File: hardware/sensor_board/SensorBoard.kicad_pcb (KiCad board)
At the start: 2 copper layers, 89.5 x 80 mm, 26 parts, among them J1 EXT, J10 LED L1, J11 LED R3, J12 LED R2, J13 LED R1, J14 HX711 L, J15 HX711 R, J2 TARE L, J3 TARE R, J4 SOIL SENSOR L, J5 SOIL SENSOR R, J6 DHT22 L, J7 DHT22 R, J8 LED L3, J9 LED L2, U1 Pico

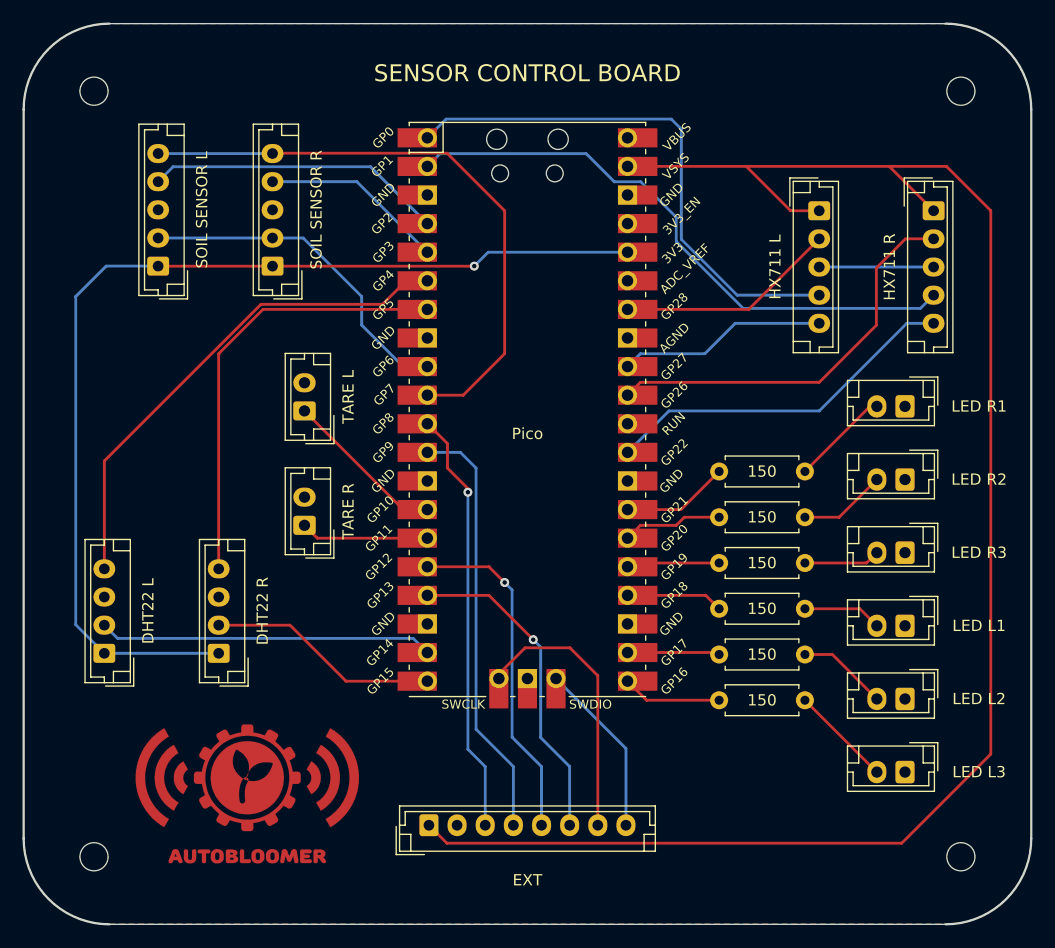
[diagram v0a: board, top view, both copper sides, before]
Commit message: PCB v2.0. Using sonars instead of load cells, which frees up the tare buttons. Also using a shift register for LEDs instead of direct GPIO control which frees up three more pins.
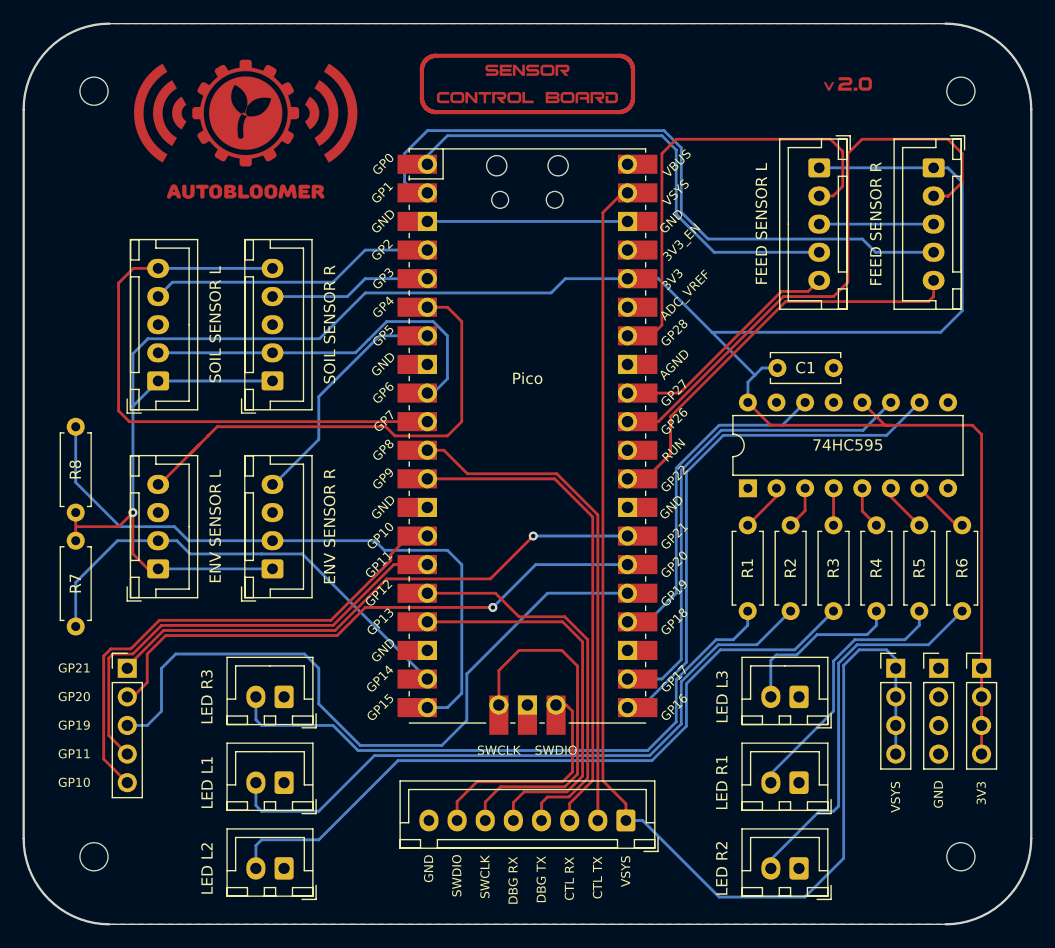
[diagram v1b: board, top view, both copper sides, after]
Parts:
- removed the J2 at (114.3, 83.8)
- removed the J3 at (114.3, 94.0)
- added C1: 0.1uf, Capacitor_THT:C_Disc_D6.0mm_W2.5mm_P5.00mm, F.Cu at (156.3, 80.0)
- added J14: SPARE GPIO, Connector_PinHeader_2.54mm:PinHeader_1x05_P2.54mm_Vertical, F.Cu at (98.6, 106.7)
- added J15: VSYS BUS, Connector_PinHeader_2.54mm:PinHeader_1x04_P2.54mm_Vertical, F.Cu at (166.8, 106.7)
- added J16: GND BUS, Connector_PinHeader_2.54mm:PinHeader_1x04_P2.54mm_Vertical, F.Cu at (170.6, 106.7)
- added J17: 3V3 BUS, Connector_PinHeader_2.54mm:PinHeader_1x04_P2.54mm_Vertical, F.Cu at (174.4, 106.7)
- added R7: R7, Resistor_THT:R_Axial_DIN0207_L6.3mm_D2.5mm_P7.62mm_Horizontal, F.Cu at (94.0, 103.0)
- added R8: R8, Resistor_THT:R_Axial_DIN0207_L6.3mm_D2.5mm_P7.62mm_Horizontal, F.Cu at (94.0, 85.2)
- added U2: 74HC595, Package_DIP:DIP-16_W7.62mm, F.Cu at (153.7, 90.7)
- J1: footprint Connector_JST:JST_EH_B8B-EH-A_1x08_P2.50mm_Vertical -> Connector_JST:JST_XH_B8B-XH-A_1x08_P2.50mm_Vertical
- J10: renamed from J11; value LED R3 -> LED L2; footprint Connector_JST:JST_EH_B2B-EH-A_1x02_P2.50mm_Vertical -> Connector_JST:JST_XH_B2B-XH-A_1x02_P2.50mm_Vertical
- J11: renamed from J10; value LED L1 -> LED L3; footprint Connector_JST:JST_EH_B2B-EH-A_1x02_P2.50mm_Vertical -> Connector_JST:JST_XH_B2B-XH-A_1x02_P2.50mm_Vertical
- J12: renamed from J9; value LED L2 -> LED R1; footprint Connector_JST:JST_EH_B2B-EH-A_1x02_P2.50mm_Vertical -> Connector_JST:JST_XH_B2B-XH-A_1x02_P2.50mm_Vertical
- J13: renamed from J8; value LED L3 -> LED R2; footprint Connector_JST:JST_EH_B2B-EH-A_1x02_P2.50mm_Vertical -> Connector_JST:JST_XH_B2B-XH-A_1x02_P2.50mm_Vertical
- J2: renamed from J4; footprint Connector_JST:JST_EH_B5B-EH-A_1x05_P2.50mm_Vertical -> Connector_JST:JST_XH_B5B-XH-A_1x05_P2.50mm_Vertical
- J3: renamed from J5; footprint Connector_JST:JST_EH_B5B-EH-A_1x05_P2.50mm_Vertical -> Connector_JST:JST_XH_B5B-XH-A_1x05_P2.50mm_Vertical
- J4: renamed from J6; value DHT22 L -> ENV SENSOR L; footprint Connector_JST:JST_EH_B4B-EH-A_1x04_P2.50mm_Vertical -> Connector_JST:JST_XH_B4B-XH-A_1x04_P2.50mm_Vertical
- J5: renamed from J7; value DHT22 R -> ENV SENSOR R; footprint Connector_JST:JST_EH_B4B-EH-A_1x04_P2.50mm_Vertical -> Connector_JST:JST_XH_B4B-XH-A_1x04_P2.50mm_Vertical
- J6: renamed from J14; value HX711 L -> FEED SENSOR L; footprint Connector_JST:JST_EH_B5B-EH-A_1x05_P2.50mm_Vertical -> Connector_JST:JST_XH_B5B-XH-A_1x05_P2.50mm_Vertical
- J7: renamed from J15; value HX711 R -> FEED SENSOR R; footprint Connector_JST:JST_EH_B5B-EH-A_1x05_P2.50mm_Vertical -> Connector_JST:JST_XH_B5B-XH-A_1x05_P2.50mm_Vertical
- J8: renamed from J13; value LED R1 -> LED R3; footprint Connector_JST:JST_EH_B2B-EH-A_1x02_P2.50mm_Vertical -> Connector_JST:JST_XH_B2B-XH-A_1x02_P2.50mm_Vertical
- J9: renamed from J12; value LED R2 -> LED L1; footprint Connector_JST:JST_EH_B2B-EH-A_1x02_P2.50mm_Vertical -> Connector_JST:JST_XH_B2B-XH-A_1x02_P2.50mm_Vertical
- R1: value 150 -> R1
- R2: value 150 -> R2
- R3: value 150 -> R3
- R4: value 150 -> R4
- R5: value 150 -> R5
- R6: value 150 -> R6
- moved J10 61.9 mm to (112.5, 124.5)
- moved J9 61.4 mm to (112.5, 116.8)
- moved J8 60.9 mm to (112.5, 109.2)
- moved R6 26.6 mm to (172.7, 94.0), turned to -90 degrees
- moved R5 21.2 mm to (168.9, 94.0), turned to -90 degrees
- moved J1 17.5 mm to (142.9, 120.2), turned to 180 degrees
- moved R4 15.8 mm to (165.1, 94.0), turned to -90 degrees
- moved J13 12.7 mm to (158.2, 124.5)
- moved J12 12.0 mm to (158.2, 116.8)
- moved J11 11.3 mm to (158.2, 109.2)
- moved R3 10.7 mm to (161.3, 94.0), turned to -90 degrees
- moved J2 10.2 mm to (101.3, 81.2)
- moved J3 10.2 mm to (111.5, 81.2)
- moved J4 8.89 mm to (101.3, 97.8)
- moved J5 8.89 mm to (111.5, 97.8)
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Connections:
- net Net-(J14-Pad2) renamed /FEED SENSOR L TX
- net Net-(J14-Pad4) renamed /FEED SENSOR L DETECT
- net Net-(J14-Pad5) renamed /FEED SENSOR L RX
- net Net-(J15-Pad2) renamed /FEED SENSOR R TX
- net Net-(J15-Pad4) renamed /FEED SENSOR R DETECT
- net Net-(J15-Pad5) renamed /FEED SENSOR R RX
- net Net-(J4-Pad2) renamed /I2C1 SDA
- net Net-(J4-Pad4) renamed /SOIL SENSOR L DETECT
- net Net-(J4-Pad5) renamed /I2C1 SCL
- net Net-(J5-Pad4) renamed /SOIL SENSOR R DETECT
- net Net-(J6-Pad2) renamed /ENV SENSOR L CTL
- net Net-(J6-Pad4) renamed /ENV SENSOR L DETECT
- net Net-(J7-Pad2) renamed /ENV SENSOR R CTL
- net Net-(J7-Pad4) renamed /ENV SENSOR R DETECT
- J1 pad 2: GND -> /CTL TX
- J1 pad 3: Net-(J1-Pad3) -> /CTL RX
- J1 pad 4: Net-(J1-Pad4) -> /DBG TX
- J1 pad 5: Net-(J1-Pad5) -> /DBG RX
- J1 pad 6: Net-(J1-Pad6) -> /SWCLK
- J1 pad 7: Net-(J1-Pad7) -> /SWDIO
- J1 pad 8: Net-(J1-Pad8) -> GND
- J2 pad 1: +3.3V -> +3V3
- J3 pad 1: +3.3V -> +3V3
- J4 pad 1: +3.3V -> +3V3
- J5 pad 1: +3.3V -> +3V3
- J6 pad 1: VS -> +3V3
- J7 pad 1: VS -> +3V3
- U1 pad 11: Net-(J1-Pad3) -> /CTL TX
- U1 pad 12: Net-(J1-Pad4) -> /CTL RX
- U1 pad 14: Net-(J2-Pad1) -> /GPIO10
- U1 pad 15: Net-(J3-Pad1) -> /GPIO11
- U1 pad 16: Net-(J1-Pad5) -> /DBG TX
- U1 pad 17: Net-(J1-Pad6) -> /DBG RX
- U1 pad 21: Net-(R6-Pad1) -> Net-(U1-Pad21)
- U1 pad 22: Net-(R5-Pad1) -> Net-(U1-Pad22)
- U1 pad 24: Net-(R4-Pad1) -> Net-(U1-Pad24)
- U1 pad 25: Net-(R3-Pad1) -> /GPIO19
- U1 pad 26: Net-(R2-Pad1) -> /GPIO20
- U1 pad 27: Net-(R1-Pad1) -> /GPIO21
- U1 pad 36: +3.3V -> +3V3
- U1 pad 41: Net-(J1-Pad7) -> /SWCLK
- U1 pad 43: Net-(J1-Pad8) -> /SWDIO
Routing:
- net +3V3: track 0.00 -> 221.2 mm, vias 0 -> 1
- net +3.3V: track 93.5 -> 0.00 mm, vias 1 -> 0
- net /GPIO19: track 0.00 -> 62.5 mm
- net Net-(J10-Pad2): track 6.77 -> 64.2 mm
- net Net-(J9-Pad2): track 7.78 -> 59.3 mm
- net /GPIO20: track 0.00 -> 50.3 mm, vias 0 -> 1
- net /GPIO21: track 0.00 -> 49.2 mm, vias 0 -> 1
- net Net-(U1-Pad21): track 0.00 -> 47.0 mm
- net Net-(J8-Pad2): track 8.78 -> 54.9 mm
- net /CTL TX: track 0.00 -> 44.7 mm
- net /GPIO10: track 0.00 -> 44.0 mm
- net /CTL RX: track 0.00 -> 43.9 mm
- net Net-(U1-Pad22): track 0.00 -> 43.4 mm
- net /GPIO11: track 0.00 -> 40.9 mm
- net Net-(J1-Pad4): track 38.0 -> 0.00 mm
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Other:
- board text added: "3V3"
- board text added: "CTL RX"
- board text added: "CTL TX"
- board text added: "DBG RX"
- board text added: "DBG TX"
- board text added: "GND"
- board text added: "GP10"
- board text added: "GP11"
- board text added: "GP19"
- board text added: "GP20"
- board text added: "GP21"
- board text added: "SWCLK"
- board text added: "SWDIO"
- board text added: "VSYS"
- board text removed: "SENSOR CONTROL BOARD"

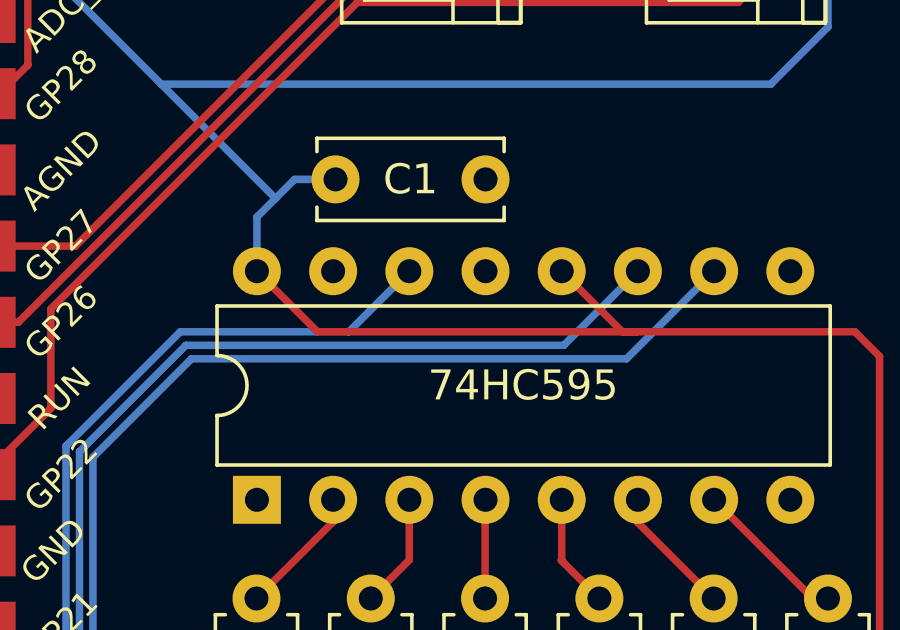
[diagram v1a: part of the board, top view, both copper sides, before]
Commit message: Fixed error in shift register wiring
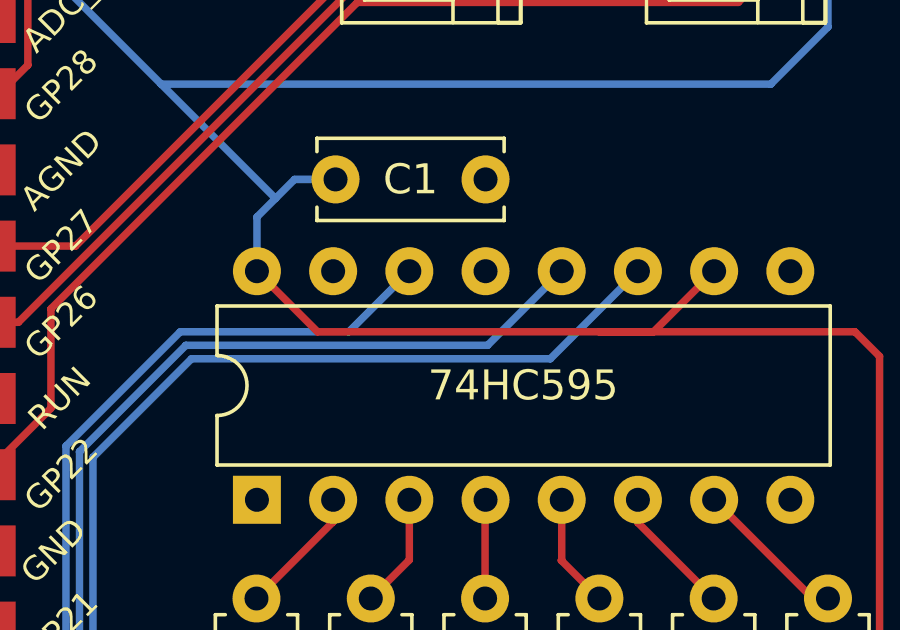
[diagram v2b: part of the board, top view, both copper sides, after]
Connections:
- U2 pad 10: Net-(U1-Pad21) -> +3V3
- U2 pad 11: Net-(U1-Pad22) -> Net-(U1-Pad21)
- U2 pad 12: +3V3 -> Net-(U1-Pad22)
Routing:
- net Net-(U1-Pad21): track 47.0 -> 44.5 mm
- net Net-(U1-Pad22): track 43.4 -> 40.9 mm
- net +3V3: track 221.2 -> 222.5 mm
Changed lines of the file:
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@@
       (net 37 "unconnected-(U2-Pad9)") (pinfunction "QH'") (pintype "output+no_connect"))
     (pad "10" thru_hole oval (at 7.62 15.24 90) (size 1.6 1.6) (drill 0.8) (layers *.Cu *.Mask)
-      (net 29 "Net-(U1-Pad21)") (pinfunction "~{SRCLR}") (pintype "input"))
+      (net 8 "+3V3") (pinfunction "~{SRCLR}") (pintype "input"))
     (pad "11" thru_hole oval (at 7.62 12.7 90) (size 1.6 1.6) (drill 0.8) (layers *.Cu *.Mask)
-      (net 30 "Net-(U1-Pad22)") (pinfunction "SRCLK") (pintype "input"))
+      (net 29 "Net-(U1-Pad21)") (pinfunction "SRCLK") (pintype "input"))
     (pad "12" thru_hole oval (at 7.62 10.16 90) (size 1.6 1.6) (drill 0.8) (layers *.Cu *.Mask)
-      (net 8 "+3V3") (pinfunction "RCLK") (pintype "input"))
+      (net 30 "Net-(U1-Pad22)") (pinfunction "RCLK") (pintype "input"))
     (pad "13" thru_hole oval (at 7.62 7.62 90) (size 1.6 1.6) (drill 0.8) (layers *.Cu *.Mask)
       (net 3 "GND") (pinfunction "~{OE}") (pintype "input"))
@@
   (segment (start 137.556948 109.943198) (end 136.64375 109.943198) (width 0.25) (layer "F.Cu") (net 7))
   (segment (start 127.85375 120.2) (end 127.85375 118.52625) (width 0.25) (layer "F.Cu") (net 7))
-  (segment (start 155.705 85.09) (end 166.37 85.09) (width 0.25) (layer "F.Cu") (net 8))
-  (segment (start 163.845 83.07) (end 165.865 85.09) (width 0.25) (layer "F.Cu") (net 8))
+  (segment (start 166.905 85.09) (end 165.1 85.09) (width 0.25) (layer "F.Cu") (net 8))
   (segment (start 173.62 85.09) (end 174.44 85.91) (width 0.25) (layer "F.Cu") (net 8))
   (segment (start 174.44 85.91) (end 174.44 107.95) (width 0.25) (layer "F.Cu") (net 8))
   (segment (start 93.98 95.35) (end 93.98 92.85) (width 0.25) (layer "F.Cu") (net 8))
   (segment (start 153.685 83.07) (end 155.705 85.09) (width 0.25) (layer "F.Cu") (net 8))
-  (segment (start 165.865 85.09) (end 166.37 85.09) (width 0.25) (layer "F.Cu") (net 8))
   (segment (start 174.44 114.3) (end 174.44 106.68) (width 0.25) (layer "F.Cu") (net 8))
   (segment (start 99.06 96.52) (end 100.39 97.85) (width 0.25) (layer "F.Cu") (net 8))
+  (segment (start 168.925 83.07) (end 166.905 85.09) (width 0.25) (layer "F.Cu") (net 8))
   (segment (start 99.06 92.85) (end 97.81 94.1) (width 0.25) (layer "F.Cu") (net 8))
+  (segment (start 165.1 85.09) (end 166.37 85.09) (width 0.25) (layer "F.Cu") (net 8))
   (segment (start 97.81 94.1) (end 94.1 94.1) (width 0.25) (layer "F.Cu") (net 8))
   (segment (start 99.06 92.71) (end 99.06 96.52) (width 0.25) (layer "F.Cu") (net 8))
   (segment (start 100.39 97.85) (end 101.3 97.85) (width 0.25) (layer "F.Cu") (net 8))
+  (segment (start 155.705 85.09) (end 165.1 85.09) (width 0.25) (layer "F.Cu") (net 8))
   (segment (start 166.37 85.09) (end 173.62 85.09) (width 0.25) (layer "F.Cu") (net 8))
   (via (at 99.06 92.85) (size 0.8) (drill 0.4) (layers "F.Cu" "B.Cu") (net 8))
@@
   (segment (start 131.031802 101.278198) (end 134.836802 97.473198) (width 0.25) (layer "B.Cu") (net 28))
   (segment (start 142.99375 110.173198) (end 144.195831 110.173198) (width 0.25) (layer "B.Cu") (net 29))
-  (segment (start 166.005 85.99) (end 168.925 83.07) (width 0.25) (layer "B.Cu") (net 29))
+  (segment (start 151.502792 85.99) (end 163.465 85.99) (width 0.25) (layer "B.Cu") (net 29))
+  (segment (start 166.385 83.07) (end 163.465 85.99) (width 0.25) (layer "B.Cu") (net 29))
   (segment (start 148.22 89.272792) (end 148.22 106.14903) (width 0.25) (layer "B.Cu") (net 29))
   (segment (start 144.195831 110.173198) (end 148.22 106.14903) (width 0.25) (layer "B.Cu") (net 29))
-  (segment (start 151.502792 85.99) (end 166.005 85.99) (width 0.25) (layer "B.Cu") (net 29))
   (segment (start 148.22 89.272792) (end 151.502792 85.99) (width 0.25) (layer "B.Cu") (net 29))
+  (segment (start 151.316396 85.54) (end 161.375 85.54) (width 0.25) (layer "B.Cu") (net 30))
   (segment (start 151.316396 85.54) (end 147.77 89.086396) (width 0.25) (layer "B.Cu") (net 30))
   (segment (start 147.77 105.913198) (end 146.05 107.633198) (width 0.25) (layer "B.Cu") (net 30))
   (segment (start 146.05 107.633198) (end 142.99375 107.633198) (width 0.25) (layer "B.Cu") (net 30))
-  (segment (start 166.385 83.07) (end 163.915 85.54) (width 0.25) (layer "B.Cu") (net 30))
-  (segment (start 163.915 85.54) (end 151.316396 85.54) (width 0.25) (layer "B.Cu") (net 30))
+  (segment (start 163.845 83.07) (end 161.375 85.54) (width 0.25) (layer "B.Cu") (net 30))
   (segment (start 147.77 89.086396) (end 147.77 105.913198) (width 0.25) (layer "B.Cu") (net 30))
   (segment (start 156.745 85.09) (end 151.13 85.09) (width 0.25) (layer "B.Cu") (net 31))
